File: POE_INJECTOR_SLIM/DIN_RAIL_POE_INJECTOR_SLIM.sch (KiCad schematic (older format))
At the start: 8 parts, among them J1 RJ45, J2 RJ45, J3 Conn_01x02_Female, J4 Conn_01x01_Male, J5 Conn_01x01_Male

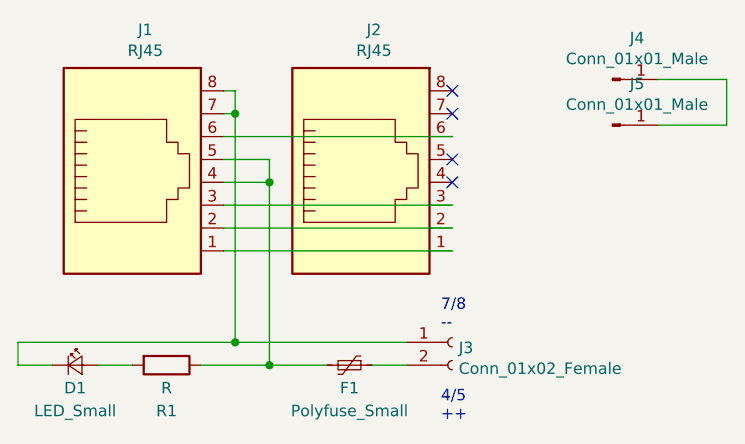
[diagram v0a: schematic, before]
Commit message: resistor and polyswitch values
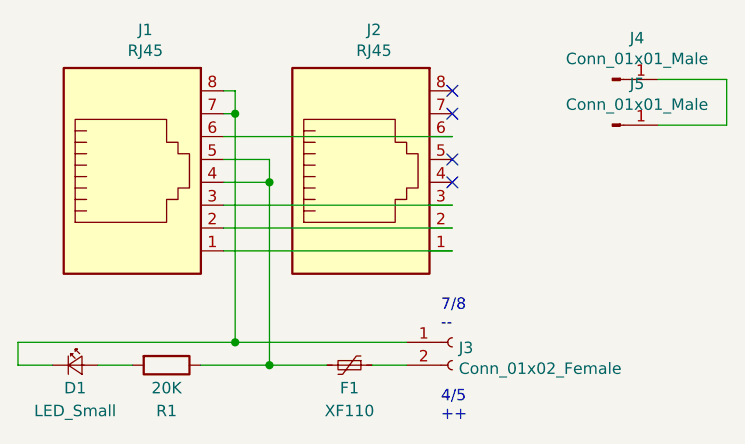
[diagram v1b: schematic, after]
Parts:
- F1: value Polyfuse_Small -> XF110
- R1: value R -> 20K
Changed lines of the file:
@@
 P 3500 3700
 F 0 "R1" V 3700 3700 50  0000 C CNN
-F 1 "R" V 3600 3700 50  0000 C CNN
+F 1 "20K" V 3600 3700 50  0000 C CNN
 F 2 "Resistor_THT:R_Axial_DIN0204_L3.6mm_D1.6mm_P2.54mm_Vertical" V 3430 3700 50  0001 C CNN
 F 3 "~" H 3500 3700 50  0001 C CNN
@@
 P 4300 3700
 F 0 "F1" V 4400 3700 50  0000 C CNN
-F 1 "Polyfuse_Small" V 4500 3700 50  0000 C CNN
+F 1 "XF110" V 4500 3700 50  0000 C CNN
 F 2 "Capacitor_THT:C_Disc_D4.3mm_W1.9mm_P5.00mm" H 4350 3500 50  0001 L CNN
 F 3 "~" H 4300 3700 50  0001 C CNN
